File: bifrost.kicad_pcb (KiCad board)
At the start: 2 copper layers, 73.7 x 71.1 mm, 71 parts, among them J1 395430002, J10 Conn_0.1_01x04, J11 Conn_0.1_01x06, J12 Micro_SD_Card_Det_Single, J2 395430002, J3 393570003, J4 393570003, J5 393570003, J6 393570003, J7 SJ_3524, J8 Conn_0.1_01x03, J9 Conn_0.1_01x04, SW1 SW_Push, SW2 SW_Push, SW3 SW_Push, SW4 SW_Push, U1 74LVC1G17, U2 74LVC1G14, U3 74AHCT125

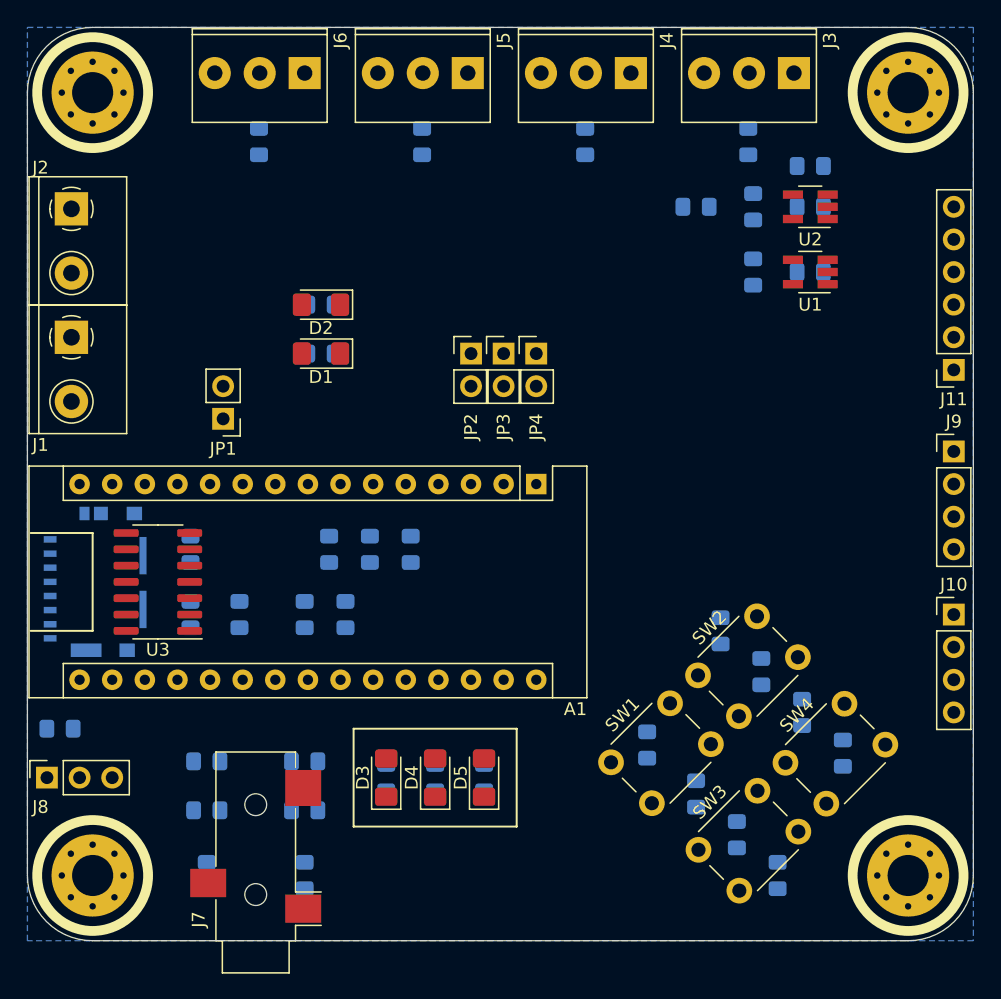
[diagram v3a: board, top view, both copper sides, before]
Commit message: Start labelling conector pins
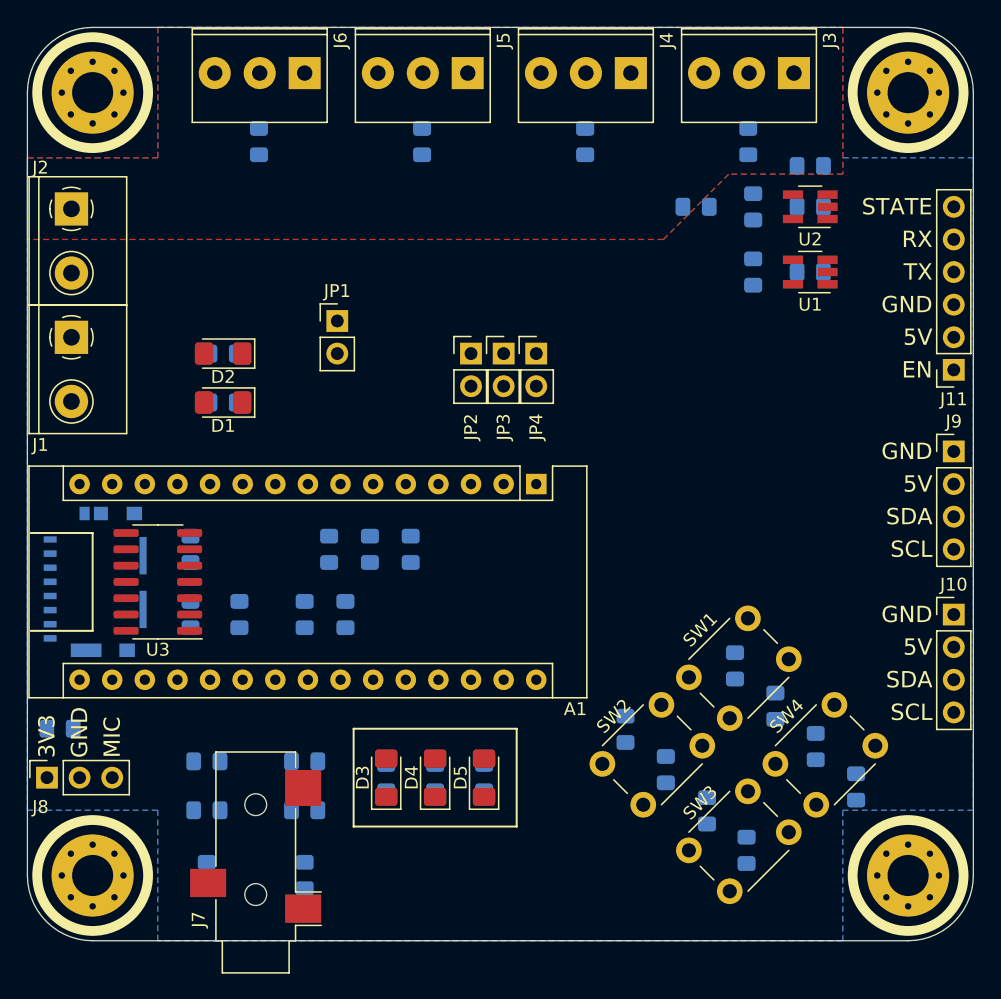
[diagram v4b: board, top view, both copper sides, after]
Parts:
- moved JP1 11.7 mm to (151.1, 76.2), turned to 0 degrees
- moved R22 10.7 mm to (173.6, 108.0), turned to 270 degrees
- moved C10 10.7 mm to (176.7, 111.1)
- moved SW2 10.1 mm to (171.8, 110.7)
- moved R21 9.21 mm to (182.1, 103.1), turned to 270 degrees
- moved C9 9.21 mm to (185.2, 106.2), turned to 270 degrees
- moved SW1 8.97 mm to (178.5, 104.0)
- moved D1 8.52 mm to (142.2, 82.5)
- moved R14 8.52 mm to (142.2, 82.5)
- moved D2 8.52 mm to (142.2, 78.7)
- moved R15 8.52 mm to (142.2, 78.7)
- moved R25 7.46 mm to (179.9, 114.3), turned to 270 degrees
- moved C12 7.17 mm to (191.5, 112.5)
- moved R26 2.17 mm to (188.4, 109.3), turned to 270 degrees
- moved C11 1.43 mm to (183.0, 117.4)
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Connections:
- A1 pad 27: /A5V -> +5V
- J2 pad 1: +5V -> VDD
- J3 pad 1: +5V -> VDD
- J4 pad 1: +5V -> VDD
- J5 pad 1: +5V -> VDD
- J6 pad 1: +5V -> VDD
- JP1 pad 1: /A5V -> VDD
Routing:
- added copper zone on F.Cu, net VDD
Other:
- board text added: "3V3"
- board text added: "5V"
- board text added: "EN"
- board text added: "GND"
- board text added: "MIC"
- board text added: "RX"
- board text added: "SCL"
- board text added: "SDA"
- board text added: "STATE"
- board text added: "TX"

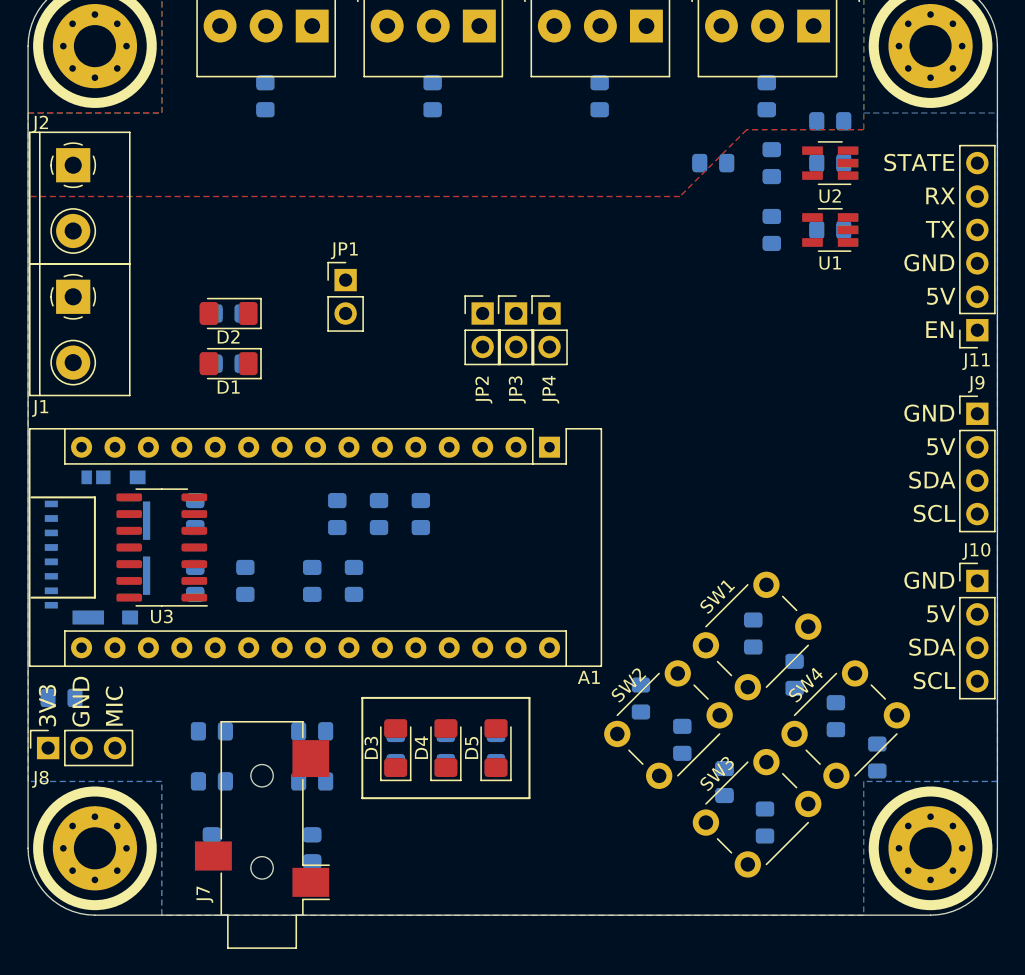
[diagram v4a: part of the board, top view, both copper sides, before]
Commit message: Continue labelling and start routing
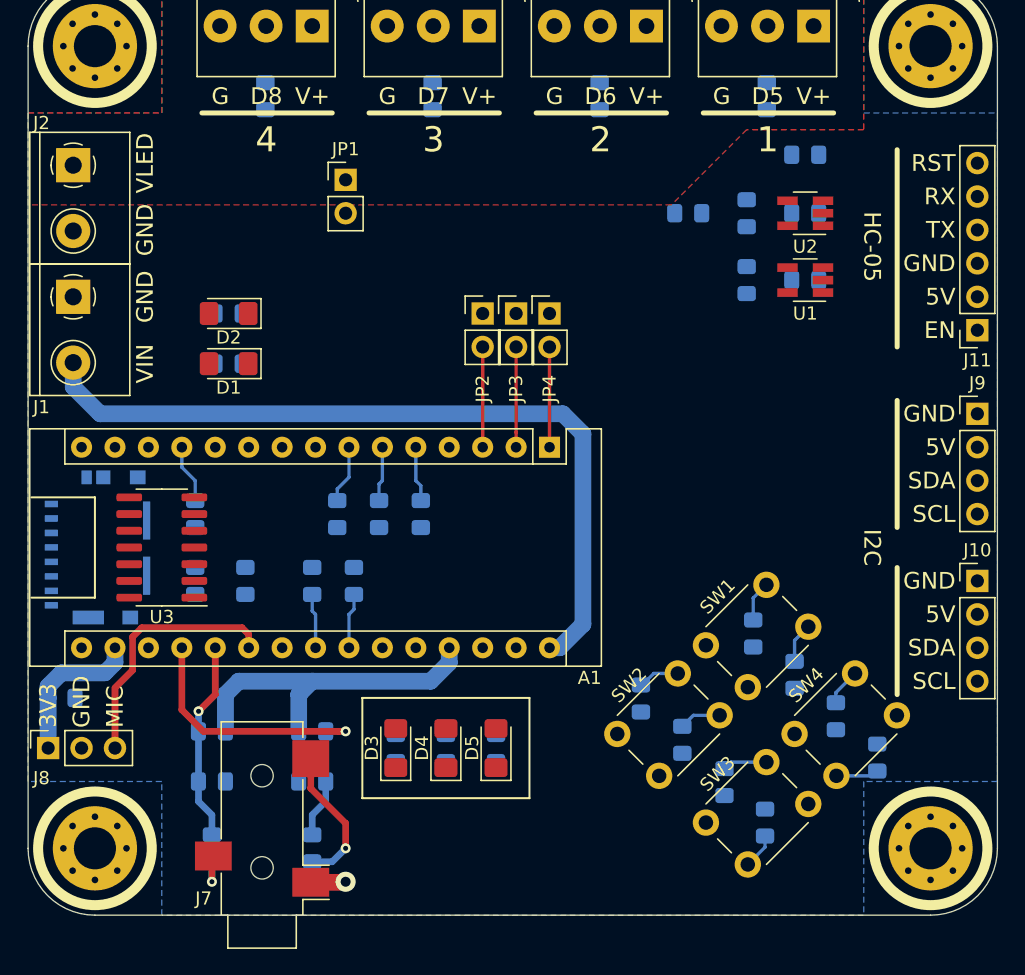
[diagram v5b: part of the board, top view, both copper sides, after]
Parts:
- moved JP1 7.62 mm to (151.1, 68.6)
- moved C2 4.26 mm to (186.1, 76.2)
- moved C3 4.26 mm to (177.2, 71.1)
- moved C4 4.26 mm to (186.1, 71.1)
- moved U1 4.26 mm to (186.1, 76.2)
- moved U2 4.26 mm to (186.1, 71.1)
- moved R1 4.26 mm to (181.6, 76.2)
- moved R2 4.26 mm to (181.6, 71.1)
- moved R9 3.17 mm to (186.1, 66.7)
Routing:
- net VBUS: track 0.00 -> 59.8 mm
- net /AUD_L: track 0.00 -> 27.6 mm, vias 0 -> 1
- net +5V: track 0.00 -> 26.2 mm
- net /MIC_IN: track 0.00 -> 19.7 mm
- net /AUD_R: track 0.00 -> 15.2 mm, vias 0 -> 1
- net +3V3: track 0.00 -> 11.7 mm
- net /AUD_IN_L: track 0.00 -> 10.9 mm, vias 0 -> 1
- net /BTN4: track 0.00 -> 7.73 mm
- net Net-(A1-Pad3): track 0.00 -> 7.62 mm
- net Net-(A1-Pad2): track 0.00 -> 7.62 mm
- net Net-(A1-Pad1): track 0.00 -> 7.62 mm
- net /BTN3: track 0.00 -> 7.61 mm
- net /BTN1: track 0.00 -> 7.28 mm
- net /BTN2: track 0.00 -> 6.86 mm
- net /I2C_SCL: track 0.00 -> 4.21 mm
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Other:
- net class AnalogSignal added: clearance 0.1524, trace_width 0.508, via_dia 0.762, via_drill 0.381
- net class Default: clearance 0.2 -> 0.1524; trace_width 0.25 -> 0.254; via_dia 0.8 -> 0.762; via_drill 0.4 -> 0.381
- net class LowPower added: clearance 0.254, trace_width 0.762, via_dia 1.016, via_drill 0.508
- net class Power added: clearance 0.254, trace_width 1.27, via_dia 1.524, via_drill 0.762
- rule trace_clearance: 0.2 -> 0.1524
- rule trace_min: 0.2 -> 0.1524
- rule via_min_drill: 0.3 -> 0.127
- rule via_min_size: 0.4 -> 0.381
- board text added: "1"
- board text added: "2"
- board text added: "3"
- board text added: "4"
- board text added: "D5"
- board text added: "D6"
- board text added: "D7"
- board text added: "D8"
- board text added: "G"
- board text added: "HC-05"
- board text added: "I2C"
- board text added: "RST"
- board text added: "V+"
- board text added: "VIN"
- board text added: "VLED"
- board text removed: "STATE"

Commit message: Continue routing
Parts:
- moved D2 9.67 mm to (138.4, 69.8), turned to 90 degrees
- moved R15 9.67 mm to (138.4, 69.8), turned to 90 degrees
- moved D1 4.58 mm to (138.4, 80.0), turned to 270 degrees
- moved R14 4.58 mm to (138.4, 80.0), turned to 270 degrees
- moved C7 1.27 mm to (148.6, 118.1), turned to 180 degrees
- moved C8 1.27 mm to (141.0, 118.1), turned to 0 degrees
- moved J12 0.25 mm to (128.5, 93.0)
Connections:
- D2 pad 2: +5V -> VDD
- U3 pad 11: Net-(U3-Pad11) -> Net-(J12-Pad5)
- U3 pad 12: GND -> /SCK
- U3 pad 2: /SCK -> GND
- U3 pad 3: Net-(J12-Pad5) -> Net-(U3-Pad3)
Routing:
- net Net-(J12-Pad3): track 0.00 -> 26.2 mm, vias 0 -> 1
- net GND: track 2.67 -> 19.2 mm, vias 1 -> 3
- net +3V3: track 11.7 -> 27.9 mm
- net /MOSI: track 0.00 -> 13.9 mm
- net /MISO: track 0.00 -> 13.1 mm, vias 0 -> 1
- net /SCK: track 0.00 -> 8.63 mm
- net VBUS: track 59.8 -> 68.2 mm
- net Net-(J12-Pad2): track 0.00 -> 6.33 mm, vias 0 -> 1
- net /~CS: track 0.00 -> 6.26 mm
- net Net-(J12-Pad5): track 0.00 -> 6.11 mm, vias 0 -> 1
- net /AUD_IN_L: track 10.9 -> 6.13 mm
- net Net-(D2-Pad1): track 0.00 -> 4.09 mm, vias 0 -> 1
- net Net-(D1-Pad1): track 0.00 -> 4.09 mm, vias 0 -> 1
- net /AUD_IN_R: track 3.52 -> 5.24 mm
- net /AUD_R: track 15.2 -> 14.5 mm
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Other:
- net class IndicatorLED added: clearance 0.1524, trace_width 0.508, via_dia 0.762, via_drill 0.381

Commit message: Continue routing
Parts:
- removed the R22 at (173.6, 108.0)
- removed the R23 at (153.7, 94.0)
- added R21: 10K, Resistor_SMD:R_0805_2012Metric_Pad1.15x1.40mm_HandSolder, B.Cu at (153.7, 93.3)
- added R25: 10K, Resistor_SMD:R_0805_2012Metric_Pad1.15x1.40mm_HandSolder, B.Cu at (139.7, 93.3)
- R24: value 10K -> 100
- moved R24 45.1 mm to (179.9, 114.3), turned to 270 degrees
- moved SW2 9.52 mm to (171.8, 110.7)
- moved SW3 9.52 mm to (178.5, 117.4)
- moved R22 8.98 mm to (173.6, 108.0)
- moved C10 8.89 mm to (183.0, 117.4)
- moved C11 8.89 mm to (176.7, 111.1)
- moved C5 0.90 mm to (142.9, 99.7)
- moved R19 0.64 mm to (156.8, 93.3)
- moved R23 0.64 mm to (150.5, 93.3)
- moved C6 0.63 mm to (139.7, 99.7)
- moved R7 0.63 mm to (148.6, 99.7)
- moved R8 0.63 mm to (151.8, 99.7)
- renumbered R21 to R20, R25 to R22, R20 to R23, SW3 to SW2, SW2 to SW3
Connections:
- R24 pad 1: +5V -> Net-(R24-Pad1)
- R24 pad 2: /BTN4 -> GND
- SW3 pad 1: Net-(R22-Pad1) (its old number) -> Net-(R24-Pad1)
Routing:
- net /BTN4: track 7.73 -> 69.5 mm, vias 0 -> 3
- net /BTN3: track 7.61 -> 55.9 mm
- net +5V: track 26.2 -> 74.0 mm, vias 0 -> 3
- net /BTN1: track 7.28 -> 42.5 mm
- net /BTN2: track 6.86 -> 41.4 mm
- net Net-(R24-Pad1): track 0.00 -> 3.39 mm
- net Net-(R22-Pad1) (its old number): track 3.16 -> 0.00 mm
- net +3V3: track 27.9 -> 31.0 mm, vias 0 -> 1
- net /I2C_SDA: track 4.16 -> 3.53 mm
- net /I2C_SCL: track 4.21 -> 3.58 mm
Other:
- net class AnalogSignal: clearance 0.1524 -> 0.254
- net class Default: clearance 0.1524 -> 0.254
- net class IndicatorLED: clearance 0.1524 -> 0.254
- rule trace_clearance: 0.1524 -> 0.254
- board text added: "D"
- board text added: "L"
- board text added: "R"
- board text added: "U"

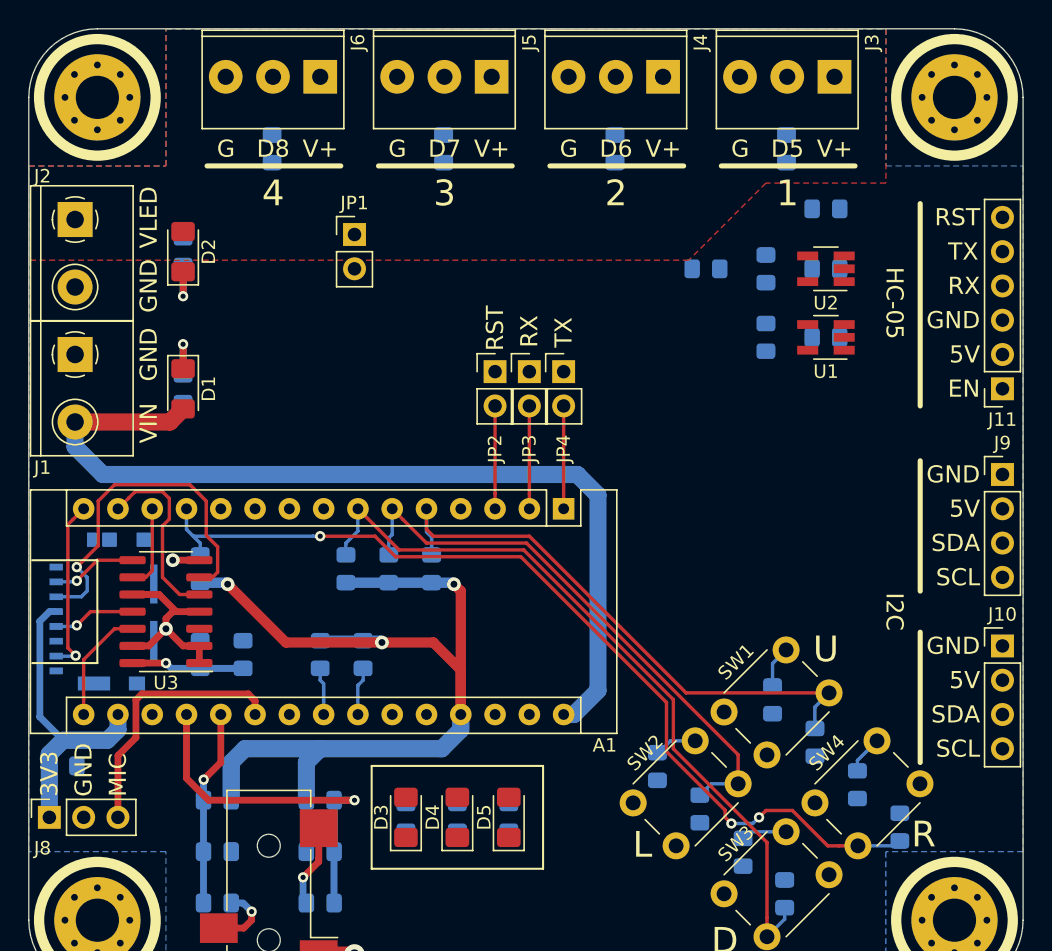
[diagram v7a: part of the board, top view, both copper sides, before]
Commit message: Finish most routing
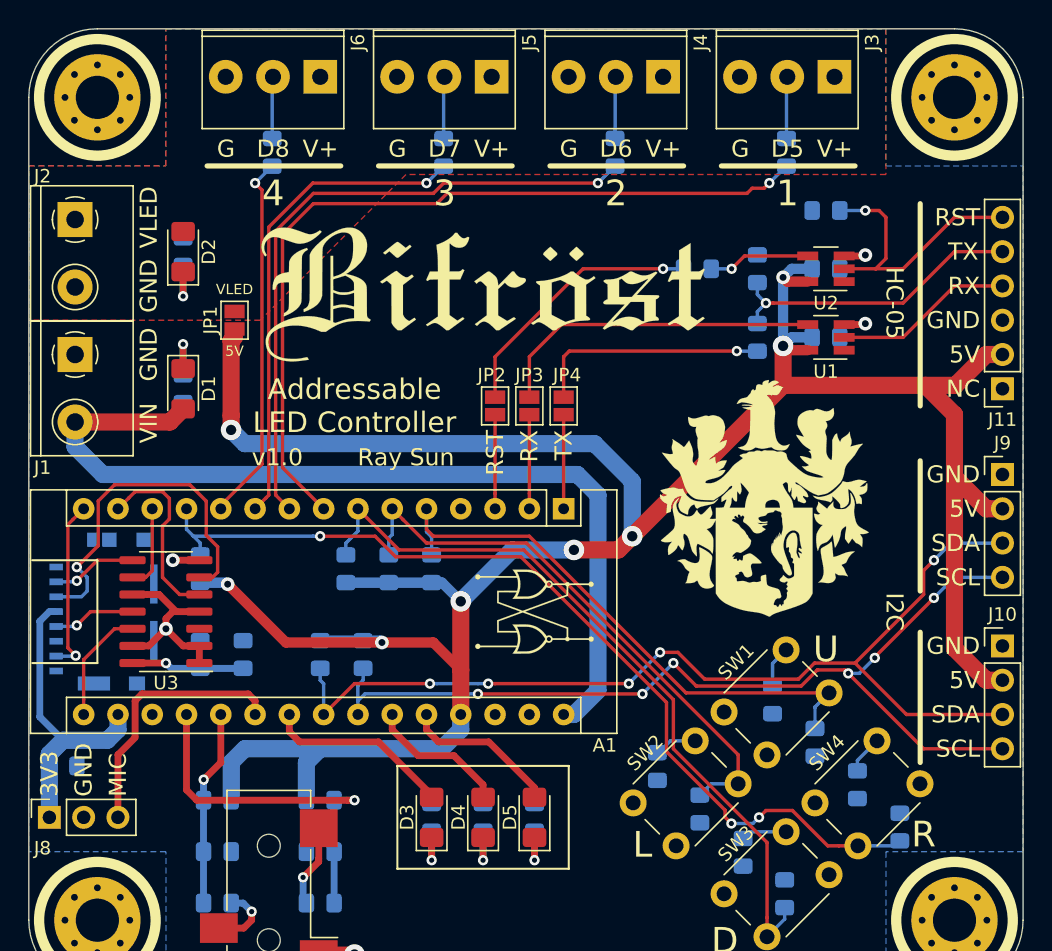
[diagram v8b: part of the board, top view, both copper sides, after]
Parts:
- added G***: LOGO, bifrost-logo:bifrost, F.Cu at (160.7, 73.0)
- added G***: LOGO, bifrost-logo:rrwb, B.Cu at (157.5, 74.9)
- added G***: LOGO, bifrost-logo:rs-s, B.Cu at (164.5, 96.5)
- added G***: LOGO, bifrost-logo:ruddock-crest, B.Cu at (181.6, 88.3)
- added G***: LOGO, bifrost-logo:ruddock-crest, F.Cu at (181.6, 88.3)
- added G***: LOGO, bifrost-logo:rs-s, F.Cu at (164.5, 96.5)
- JP1, JP2, JP3, JP4: value Jumper_NO_Small -> SolderJumper_2_Open; footprint Connector_PinHeader_2.54mm:PinHeader_1x02_P2.54mm_Vertical -> Jumper:SolderJumper-2_P1.3mm_Open_Pad1.0x1.5mm
- moved JP1 10.9 mm to (142.2, 74.9), turned to 270 degrees
- moved JP2 2.54 mm to (161.5, 81.3), turned to 90 degrees
- moved JP3 2.54 mm to (164.1, 81.3), turned to 90 degrees
- moved JP4 2.54 mm to (166.6, 81.3), turned to 90 degrees
- moved D3 1.91 mm to (156.8, 111.8)
- moved D4 1.91 mm to (160.7, 111.8)
- moved D5 1.91 mm to (164.5, 111.8)
- moved R16 1.91 mm to (156.8, 111.8)
- moved R17 1.91 mm to (160.7, 111.8)
- moved R18 1.91 mm to (164.5, 111.8)
- moved R1 0.64 mm to (181.0, 76.2)
- moved R2 0.64 mm to (181.0, 71.1)
- moved C3 0.63 mm to (176.5, 71.1)
- moved R3 0.26 mm to (183.1, 62.5)
- moved R5 0.26 mm to (157.7, 62.5)
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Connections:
- JP2 pad 1: /BT_RST -> Net-(A1-Pad3)
- JP2 pad 2: Net-(A1-Pad3) -> /BT_RST
- JP3 pad 1: Net-(JP3-Pad1) -> Net-(A1-Pad2)
- JP3 pad 2: Net-(A1-Pad2) -> Net-(JP3-Pad2)
- JP4 pad 1: Net-(JP4-Pad1) -> Net-(A1-Pad1)
- JP4 pad 2: Net-(A1-Pad1) -> Net-(JP4-Pad2)
- R1 pad 1: Net-(JP4-Pad1) -> Net-(JP4-Pad2)
- U1 pad 4: Net-(JP3-Pad1) -> Net-(JP3-Pad2)
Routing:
- net +5V: track 74.0 -> 207.1 mm, vias 3 -> 8
- net /I2C_SDA: track 3.53 -> 74.3 mm, vias 0 -> 5
- net /I2C_SCL: track 3.58 -> 70.5 mm, vias 0 -> 6
- net Net-(A1-Pad8): track 0.00 -> 61.0 mm, vias 0 -> 1
- net Net-(A1-Pad9): track 0.00 -> 48.1 mm, vias 0 -> 1
- net Net-(A1-Pad10): track 0.00 -> 36.1 mm, vias 0 -> 1
- net Net-(A1-Pad11): track 0.00 -> 27.4 mm, vias 0 -> 1
- net Net-(JP3-Pad2): track 0.00 -> 24.6 mm
- net /BT_RX: track 0.00 -> 22.7 mm, vias 0 -> 1
- net /BT_ST: track 0.00 -> 21.1 mm, vias 0 -> 1
- net /BT_RST: track 0.00 -> 19.7 mm, vias 0 -> 1
- net Net-(JP4-Pad2): track 0.00 -> 17.5 mm, vias 0 -> 1
- net /LED1: track 0.00 -> 13.9 mm
- net /BT_TX: track 0.00 -> 13.3 mm
- net /LED3: track 0.00 -> 11.6 mm
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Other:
- board text added: "Addressable LED Controller"
- board text added: "NC"
- board text added: "Ray Sun"
- board text added: "v1.0"
- board text removed: "EN"
